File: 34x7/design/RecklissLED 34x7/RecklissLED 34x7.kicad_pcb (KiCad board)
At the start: 2 copper layers, 34 x 7 mm, 6 parts

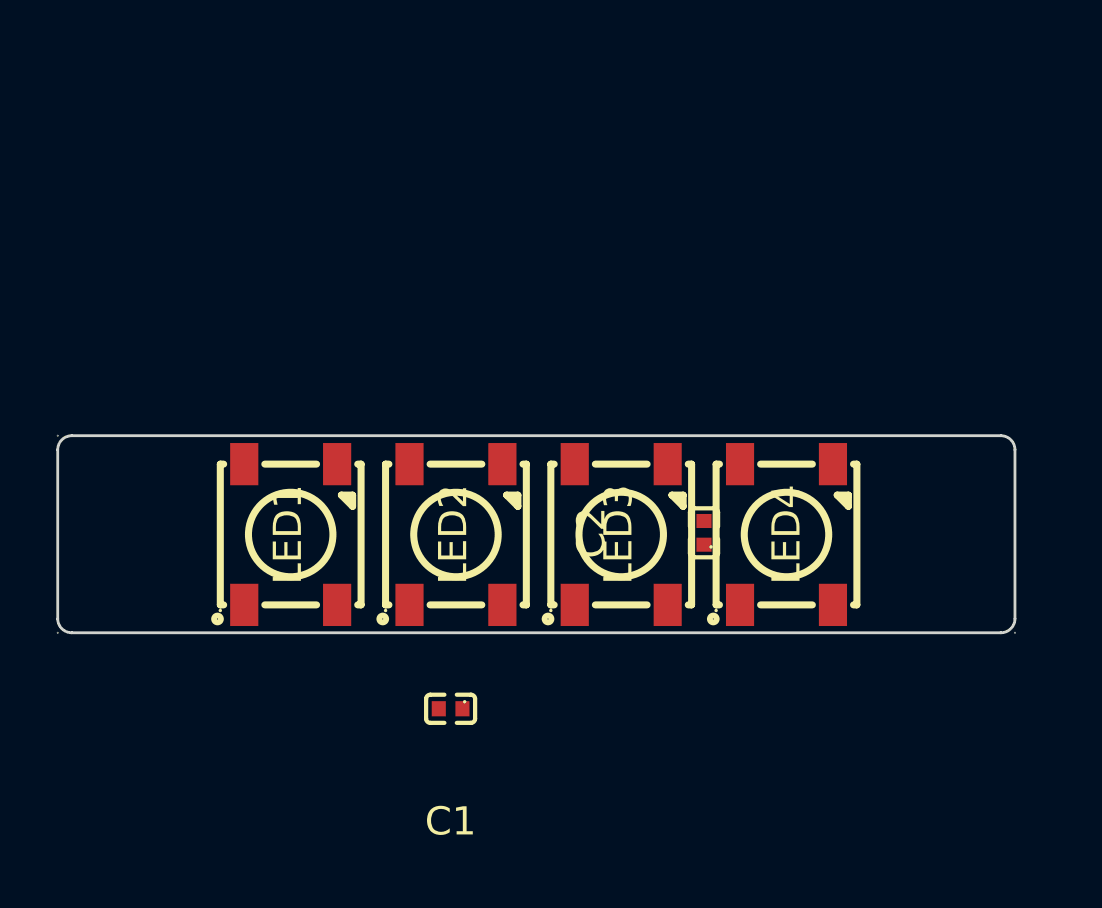
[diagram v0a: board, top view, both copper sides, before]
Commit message: Added solder pads, began schematic routing, components consolidated on pcb.
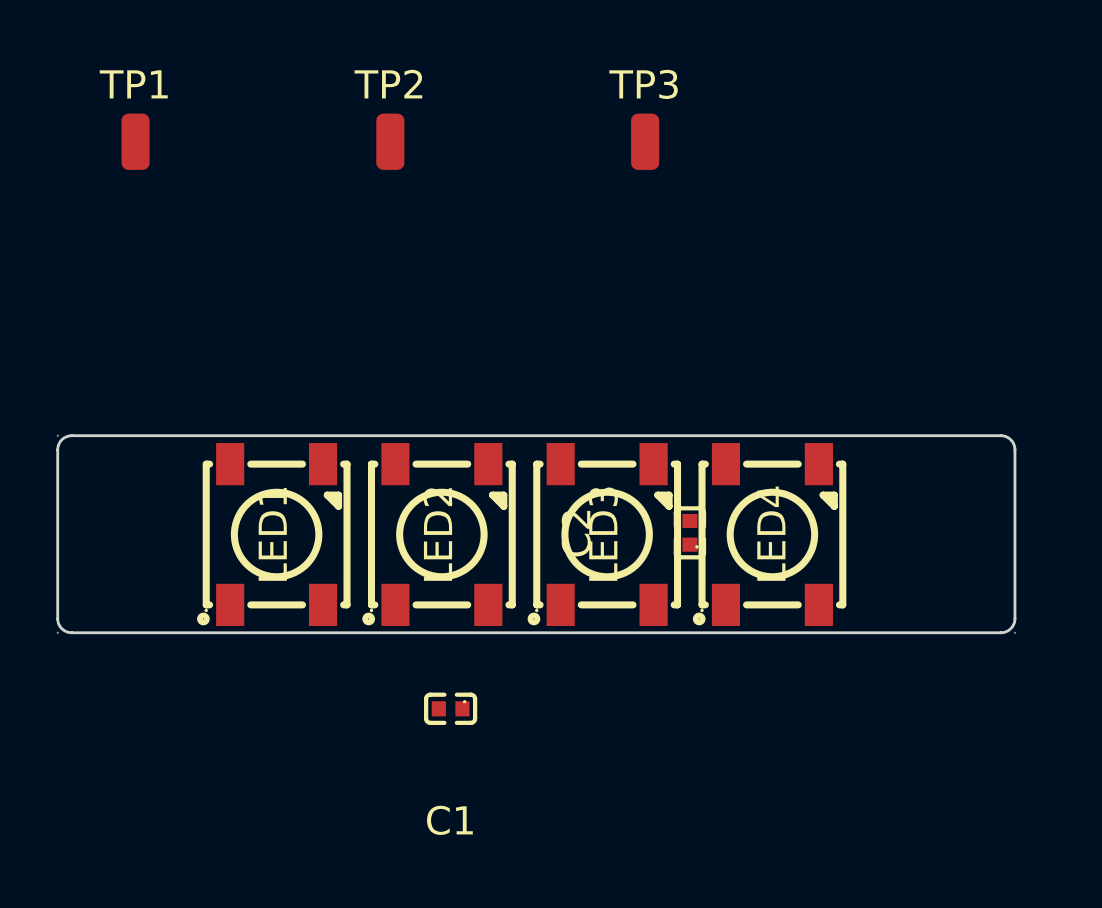
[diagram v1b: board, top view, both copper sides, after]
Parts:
- added TP1: TestPoint, Connector_Wire:SolderWirePad_1x01_SMD_1x2mm, F.Cu at (126.9, 82.0)
- added TP2: TestPoint, Connector_Wire:SolderWirePad_1x01_SMD_1x2mm, F.Cu at (135.9, 82.0)
- added TP3: TestPoint, Connector_Wire:SolderWirePad_1x01_SMD_1x2mm, F.Cu at (145.0, 82.0)
- moved C2 0.50 mm to (146.6, 95.9)
- moved LED1 0.50 mm to (131.9, 96.0)
- moved LED2 0.50 mm to (137.8, 96.0)
- moved LED3 0.50 mm to (143.7, 96.0)
- moved LED4 0.50 mm to (149.5, 96.0)
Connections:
- C1 pad 1: unconnected-(C1-Pad1) -> GND
- C1 pad 2: unconnected-(C1-Pad2) -> VBUS
- C2 pad 1: unconnected-(C2-Pad1) -> GND
- C2 pad 2: unconnected-(C2-Pad2) -> VBUS
- LED1 pad 1: unconnected-(LED1-VDD-Pad1) -> VBUS
- LED1 pad 2: unconnected-(LED1-DOUT-Pad2) -> Net-(LED1-DOUT)
- LED1 pad 3: unconnected-(LED1-VSS-Pad3) -> GND
- LED1 pad 4: unconnected-(LED1-DIN-Pad4) -> Data
- LED2 pad 1: unconnected-(LED2-VDD-Pad1) -> VBUS
- LED2 pad 2: unconnected-(LED2-DOUT-Pad2) -> Net-(LED2-DOUT)
- LED2 pad 3: unconnected-(LED2-VSS-Pad3) -> GND
- LED2 pad 4: unconnected-(LED2-DIN-Pad4) -> Net-(LED1-DOUT)
- LED3 pad 1: unconnected-(LED3-VDD-Pad1) -> VBUS
- LED3 pad 2: unconnected-(LED3-DOUT-Pad2) -> Net-(LED3-DOUT)
- LED3 pad 3: unconnected-(LED3-VSS-Pad3) -> GND
- LED3 pad 4: unconnected-(LED3-DIN-Pad4) -> Net-(LED2-DOUT)
- LED4 pad 1: unconnected-(LED4-VDD-Pad1) -> VBUS
- LED4 pad 3: unconnected-(LED4-VSS-Pad3) -> GND
- LED4 pad 4: unconnected-(LED4-DIN-Pad4) -> Net-(LED3-DOUT)

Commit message: Update schematic and pcb routing.
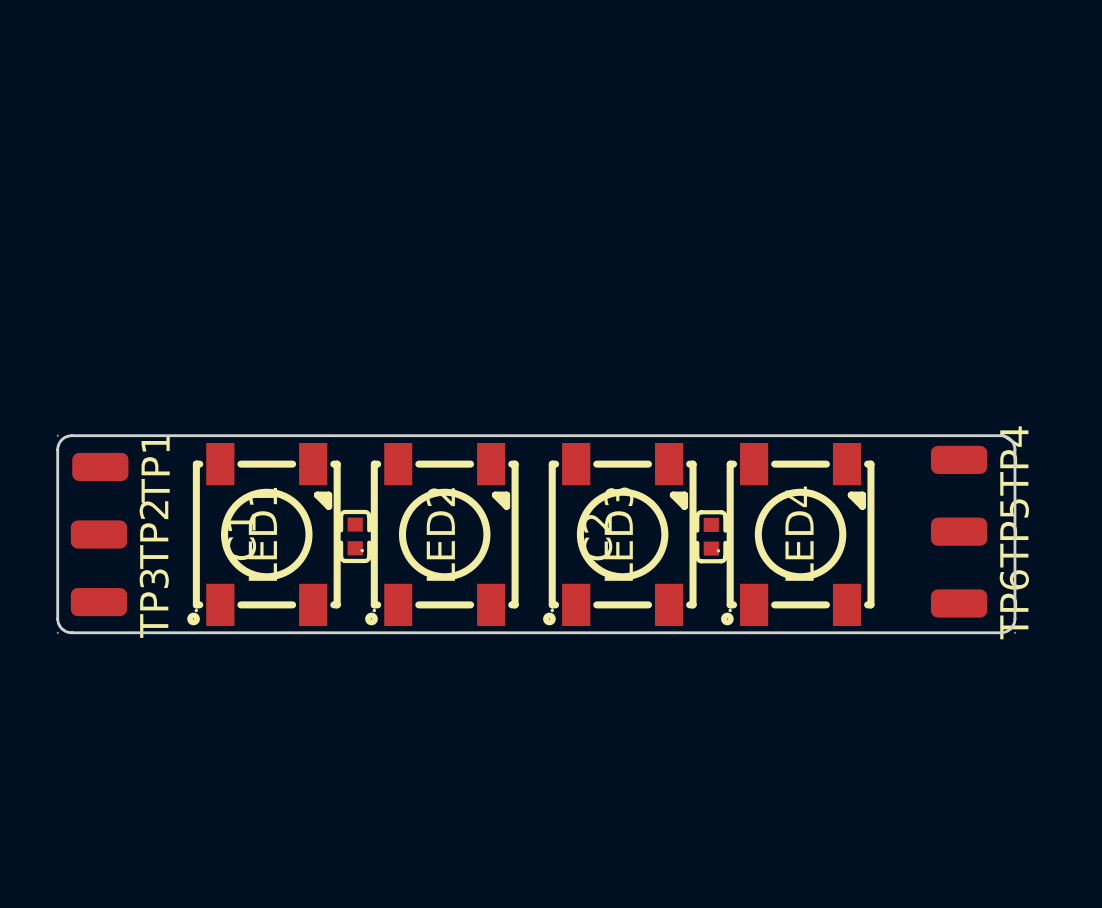
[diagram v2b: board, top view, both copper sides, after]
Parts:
- added TP4: TestPoint, Connector_Wire:SolderWirePad_1x01_SMD_1x2mm, F.Cu at (156.2, 93.3)
- added TP5: TestPoint, Connector_Wire:SolderWirePad_1x01_SMD_1x2mm, F.Cu at (156.2, 95.8)
- added TP6: TestPoint, Connector_Wire:SolderWirePad_1x01_SMD_1x2mm, F.Cu at (156.2, 98.4)
- moved TP3 25.4 mm to (125.6, 98.3), turned to -90 degrees
- moved TP2 17.3 mm to (125.6, 95.9), turned to -90 degrees
- moved TP1 11.6 mm to (125.7, 93.5), turned to -90 degrees
- moved C1 7.00 mm to (134.7, 96.0), turned to 90 degrees
- moved LED4 1.00 mm to (150.5, 96.0)
- moved C2 0.77 mm to (147.3, 96.0)
- moved LED3 0.55 mm to (144.2, 96.0)
- moved LED1 0.35 mm to (131.6, 96.0)
- moved LED2 0.10 mm to (137.9, 96.0)
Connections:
- LED4 pad 2: unconnected-(LED4-DOUT-Pad2) -> Net-(LED4-DOUT)

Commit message: All components placed on PCB
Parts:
- moved TP4 0.57 mm to (156.6, 93.6)
- moved TP6 0.43 mm to (156.6, 98.3)
- moved TP5 0.42 mm to (156.6, 95.8)
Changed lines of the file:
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@@
 	(footprint "Connector_Wire:SolderWirePad_1x01_SMD_1x2mm"
 		(layer "F.Cu")
-		(at 156.15 93.3 -90)
+		(at 156.63 93.6 -90)
 		(descr "Wire Pad, Square, SMD Pad,  1mm x 2mm")
 		(tags "MeasurementPoint Square SMDPad 1mmx2mm ")
@@
 			(at 0 -2 90)
 			(layer "F.SilkS")
+			(hide yes)
 			(effects
 				(font
@@
 	(footprint "Connector_Wire:SolderWirePad_1x01_SMD_1x2mm"
 		(layer "F.Cu")
-		(at 156.15 98.4 -90)
+		(at 156.57 98.3 -90)
 		(descr "Wire Pad, Square, SMD Pad,  1mm x 2mm")
 		(tags "MeasurementPoint Square SMDPad 1mmx2mm ")
@@
 			(at 0 -2 90)
 			(layer "F.SilkS")
+			(hide yes)
 			(effects
 				(font
@@
 	(footprint "Connector_Wire:SolderWirePad_1x01_SMD_1x2mm"
 		(layer "F.Cu")
-		(at 156.15 95.85 -90)
+		(at 156.57 95.84 -90)
 		(descr "Wire Pad, Square, SMD Pad,  1mm x 2mm")
 		(tags "MeasurementPoint Square SMDPad 1mmx2mm ")
@@
 			(at 0 -2 90)
 			(layer "F.SilkS")
+			(hide yes)
 			(effects
 				(font
@@
 		)
 		(pad "1" smd roundrect
-			(at 0 0 270)
+			(at 0.11 0 270)
 			(size 1 2)
 			(layers "F.Cu" "F.Mask")
@@
 			(at 0 -2 90)
 			(layer "F.SilkS")
+			(hide yes)
 			(effects
 				(font
@@
 			(at 0 -2 90)
 			(layer "F.SilkS")
+			(hide yes)
 			(effects
 				(font
@@
 			(at 0 -2 90)
 			(layer "F.SilkS")
-			(effects
-				(font
+			(hide yes)
+			(effects
+				(font
